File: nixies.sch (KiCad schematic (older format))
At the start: 132 parts, among them Q10 MMBTA42LT1G, Q11 MMBTA42LT1G, Q12 MMBTA42LT1G, Q13 MMBTA42LT1G, Q14 MMBTA42LT1G, Q15 MMBTA42LT1G, Q16 MMBTA42LT1G, Q17 MMBTA42LT1G, Q18 MMBTA42LT1G, Q19 MMBTA42LT1G, Q2 MMBTA42LT1G, Q20 MMBTA42LT1G, Q21 MMBTA42LT1G, Q22 MMBTA42LT1G, Q23 MMBTA42LT1G, Q24 MMBTA42LT1G, Q25 MMBTA42LT1G, Q26 MMBTA42LT1G, Q27 MMBTA42LT1G, Q28 MMBTA42LT1G, Q29 MMBTA42LT1G, Q3 MMBTA42LT1G, Q30 MMBTA42LT1G, Q31 MMBTA42LT1G, Q32 MMBTA42LT1G, Q33 MMBTA42LT1G, Q34 MMBTA42LT1G, Q35 MMBTA42LT1G, Q36 MMBTA42LT1G, Q37 MMBTA42LT1G, Q38 MMBTA42LT1G, Q39 MMBTA42LT1G, Q4 MMBTA42LT1G, Q40 MMBTA42LT1G, Q41 MMBTA42LT1G, Q42 MMBTA42LT1G, Q43 MMBTA42LT1G, Q44 MMBTA42LT1G, Q45 MMBTA42LT1G, Q46 MMBTA42LT1G, Q47 MMBTA42LT1G, Q48 MMBTA42LT1G, Q49 MMBTA42LT1G, Q5 MMBTA42LT1G, Q50 MMBTA42LT1G, Q51 MMBTA42LT1G, Q52 MMBTA42LT1G, Q53 MMBTA42LT1G, Q54 MMBTA42LT1G, Q55 MMBTA42LT1G, Q56 MMBTA42LT1G, Q57 MMBTA42LT1G, Q58 MMBTA42LT1G, Q59 MMBTA42LT1G, Q6 MMBTA42LT1G, Q60 MMBTA42LT1G, Q61 MMBTA42LT1G, Q7 MMBTA42LT1G, Q8 MMBTA42LT1G, Q9 MMBTA42LT1G

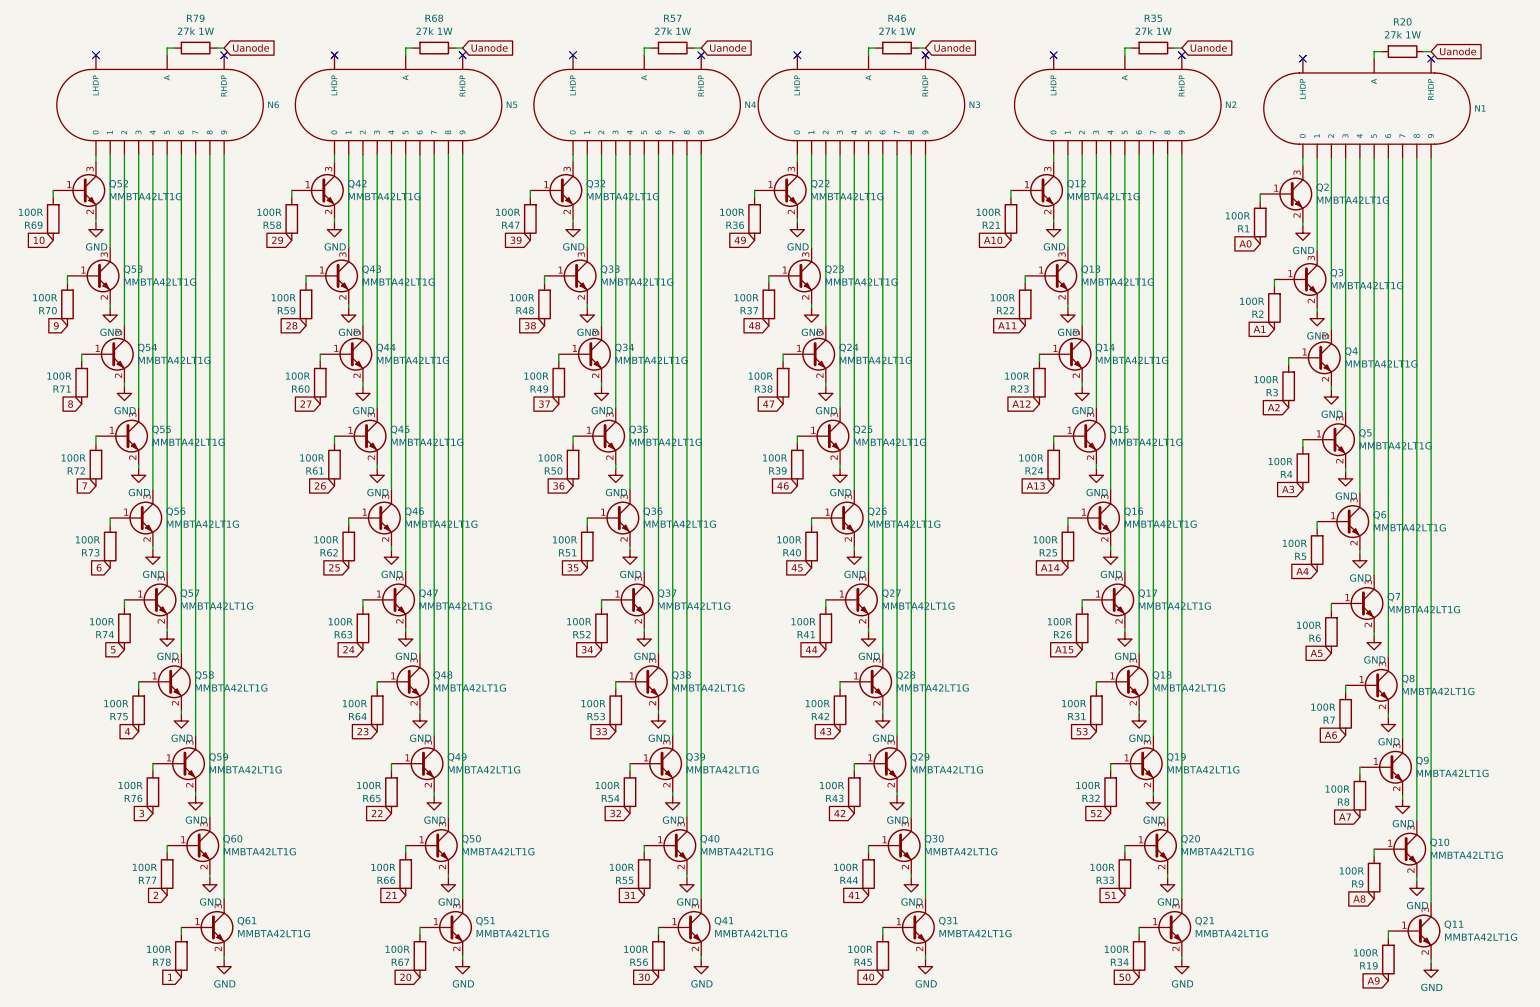
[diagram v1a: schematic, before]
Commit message: Changed BJT base resistor values, Added photo, Added new inspiration schematic, Changed README
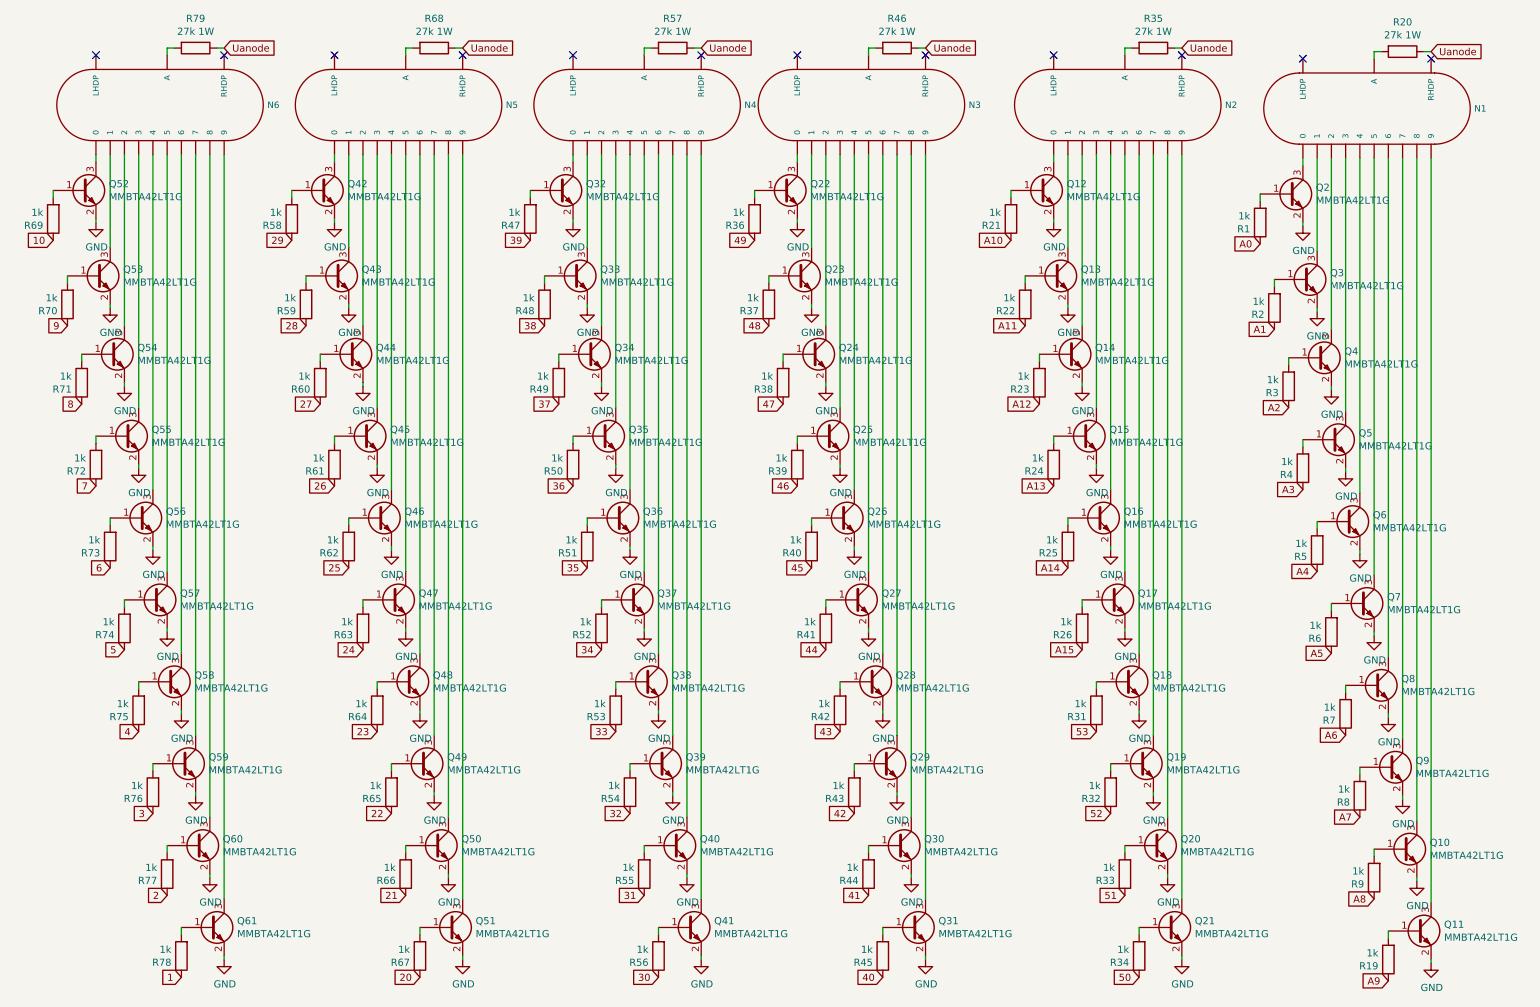
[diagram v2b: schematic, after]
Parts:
- R1, R19, R2, R21, R22, R23, R24, R25, R26, R3, R31, R32, R33, R34, R36, R37, R38, R39, R4, R40, R41, R42, R43, R44, R45, R47, R48, R49, R5, R50, R51, R52, R53, R54, R55, R56, R58, R59, R6, R60, R61, R62, R63, R64, R65, R66, R67, R69, R7, R70, R71, R72, R73, R74, R75, R76, R77, R78, R8, R9: value 100R -> 1k

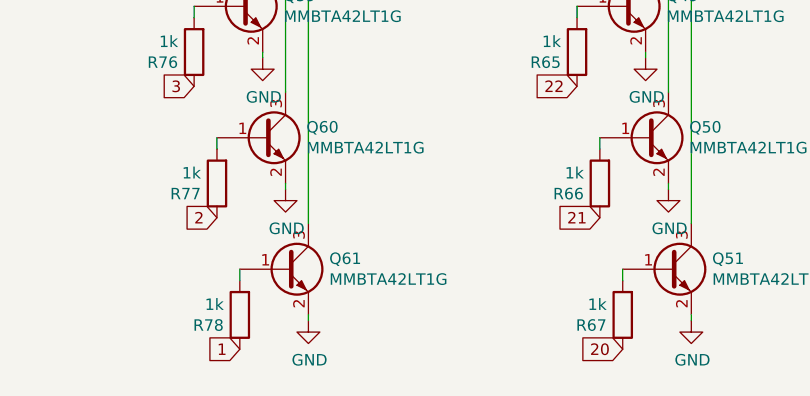
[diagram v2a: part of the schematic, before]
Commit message: Solved I2C, UART conflict
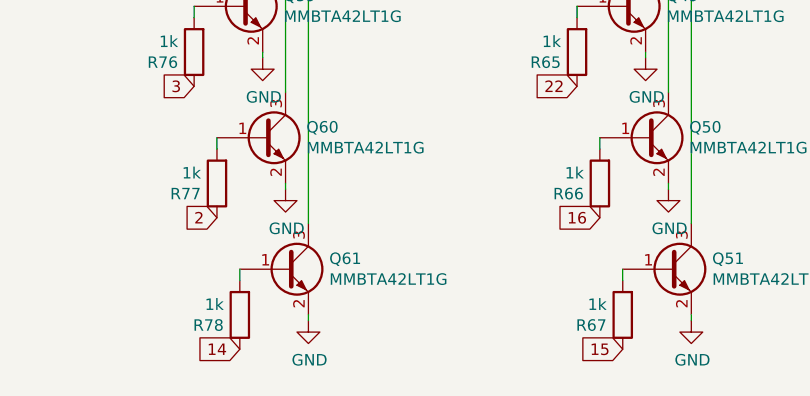
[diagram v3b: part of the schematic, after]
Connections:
- net 1 renamed 14
- net 20 renamed 15
- net 21 renamed 16
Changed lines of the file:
@@
 22
 Text GLabel 3300 6675 0    50   Input ~ 0
-21
+16
 Text GLabel 3400 7250 0    50   Input ~ 0
-20
+15
 Text GLabel 2700 3225 0    50   Input ~ 0
 27
@@
 2
 Text GLabel 1725 7250 0    50   Input ~ 0
-1
+14
 Text GLabel 1025 3225 0    50   Input ~ 0
 8
